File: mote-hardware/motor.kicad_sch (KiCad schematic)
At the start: 1 part, among them U3 TB6612FNG

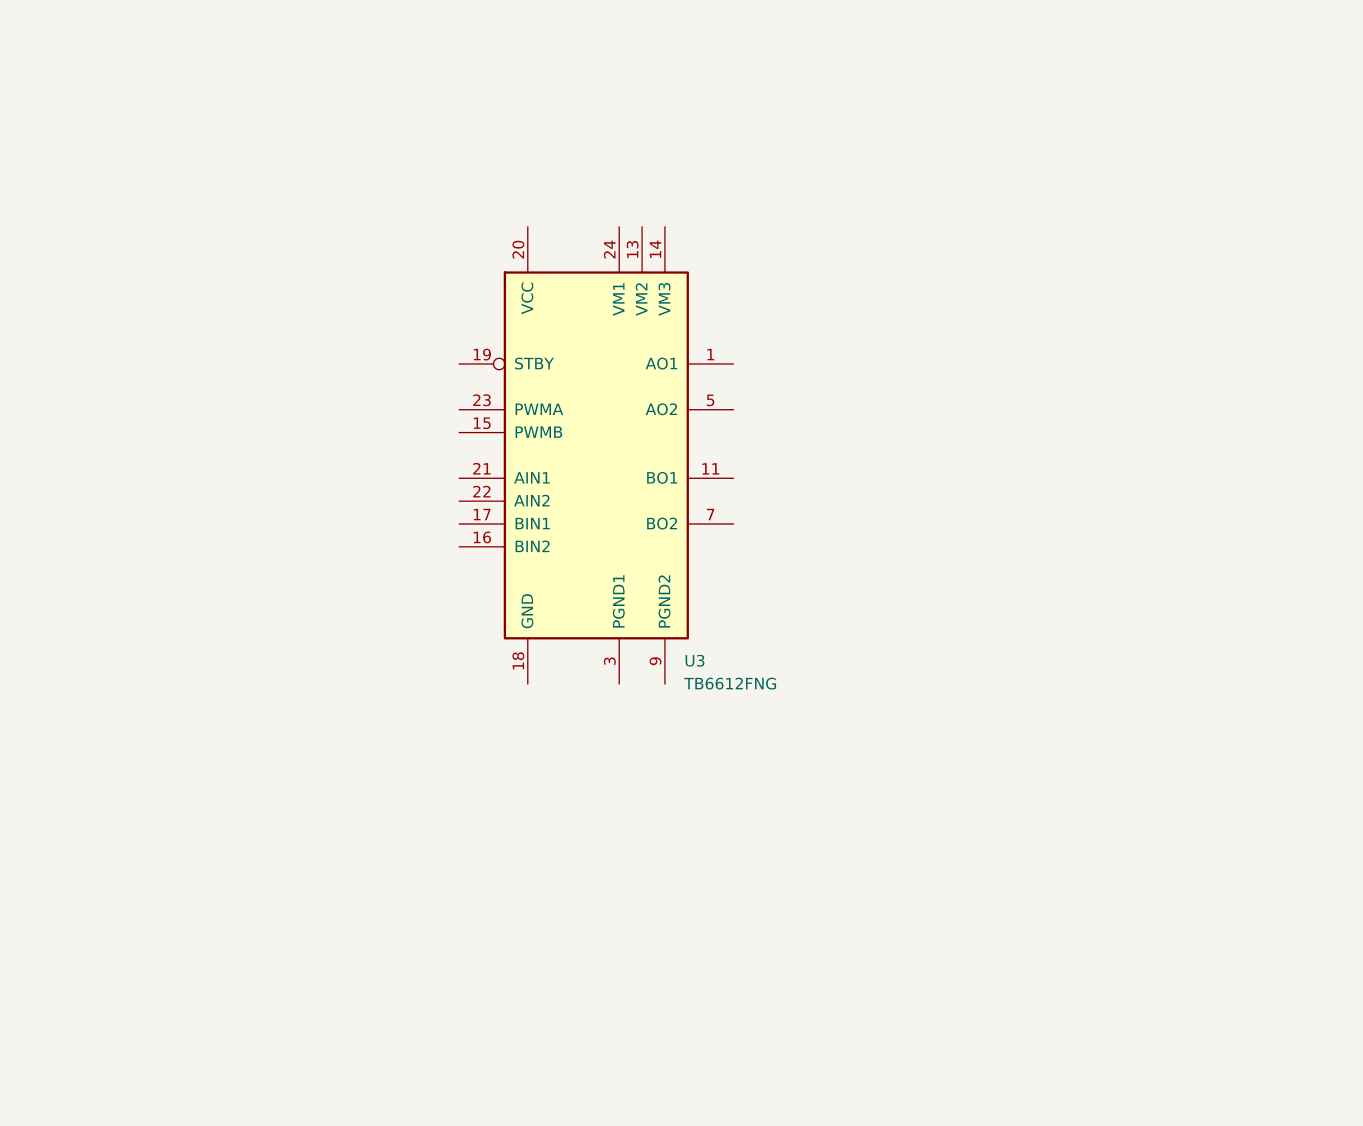
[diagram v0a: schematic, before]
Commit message: Implement motor, power, imu, status LED schematics
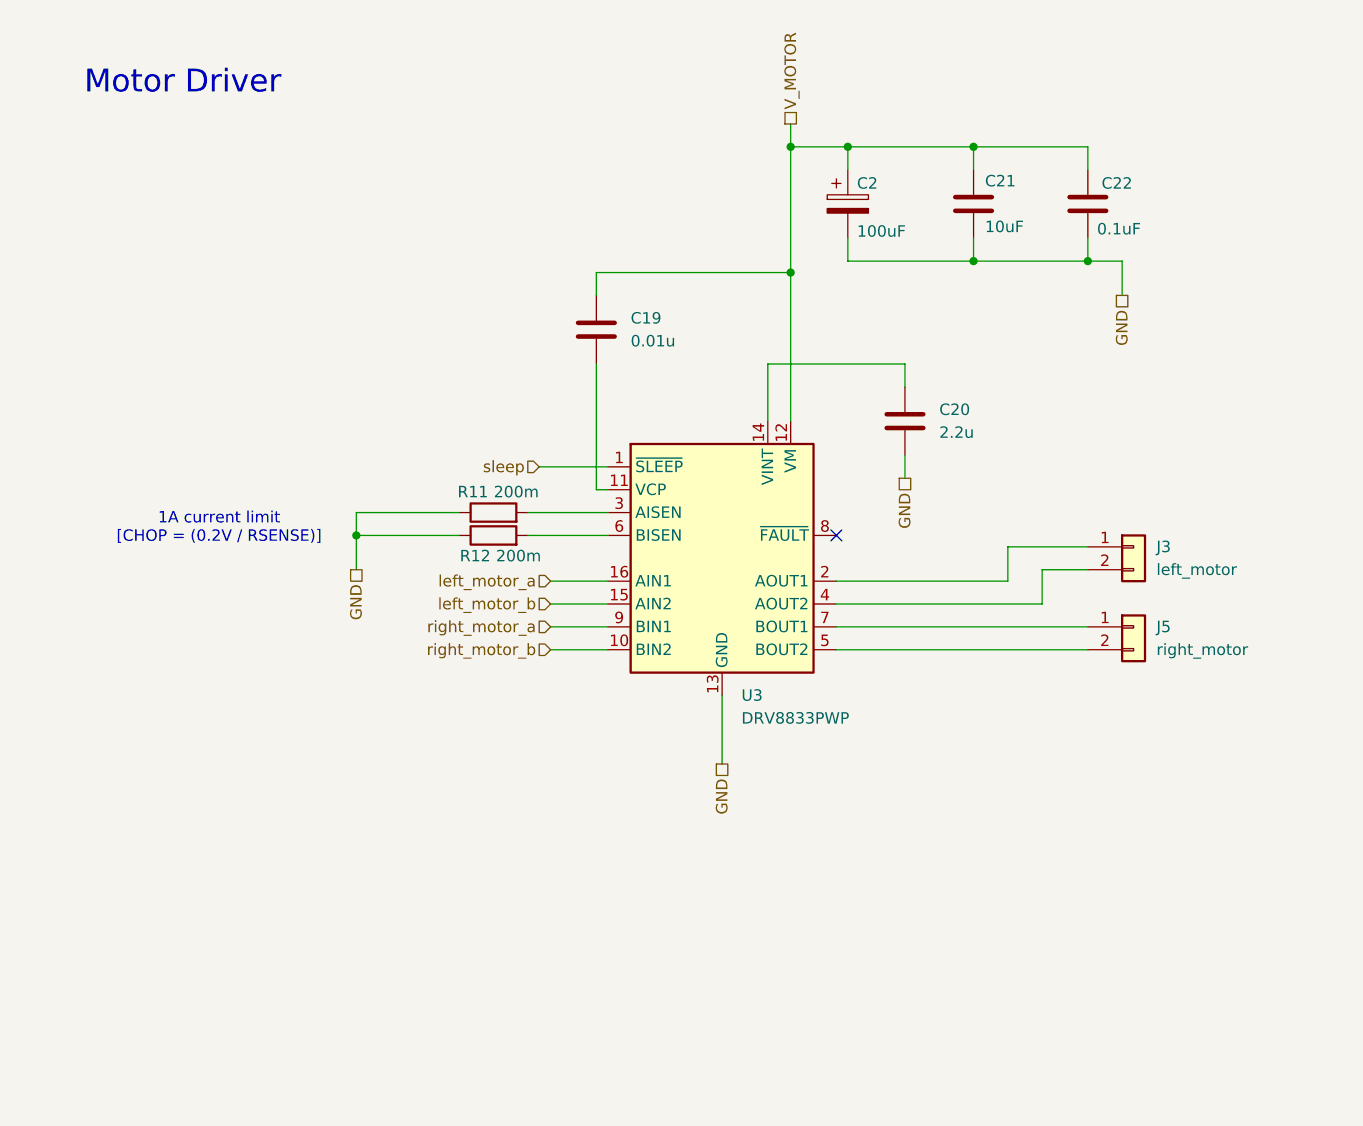
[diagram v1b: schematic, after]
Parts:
- removed U3: TB6612FNG, Package_SO:SSOP-24_5.3x8.2mm_P0.65mm, symbol Driver_Motor:TB6612FNG
- added C19: 0.01u, symbol Device:C
- added C2: 100uF, symbol Device:C_Polarized
- added C20: 2.2u, symbol Device:C
- added C21: 10uF, symbol Device:C
- added C22: 0.1uF, symbol Device:C
- added J3: left_motor, symbol Connector_Generic:Conn_01x02
- added J5: right_motor, symbol Connector_Generic:Conn_01x02
- added R11, R12: 200m, symbol Device:R
- added U3: DRV8833PWP, Package_SO:HTSSOP-16-1EP_4.4x5mm_P0.65mm_EP3.4x5mm_Mask2.46x2.31mm_ThermalVias, symbol Driver_Motor:DRV8833PWP
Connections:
- new net: J3.1 (Pin_1), U3.2 (AOUT1)
- new net: J3.2 (Pin_2), U3.4 (AOUT2)
- new net: R12.2, U3.6 (BISEN)
- new net: J5.1 (Pin_1), U3.7 (BOUT1)
- new net: J5.2 (Pin_2), U3.5 (BOUT2)
- new net: C19.1, U3.11 (VCP)
- new net: C20.2, U3.14 (VINT)
- new net: R11.2, U3.3 (AISEN)
- new net GND: C2.2, C20.1, C21.1, C22.1, R11.1, R12.1, U3.13 (GND), U3.17 (GND)
- new net V_MOTOR: C19.2, C2.1, C21.2, C22.2, U3.12 (VM)
- new net left_motor_a: U3.16 (AIN1)
- new net left_motor_b: U3.15 (AIN2)
- new net right_motor_a: U3.9 (BIN1)
- new net right_motor_b: U3.10 (BIN2)
- new net sleep: U3.1 (~{SLEEP})
- no-connect marks 0 -> 1
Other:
- note added: "1A current limit [CHOP = (0.2V / RSENSE)]"
- note added: "Motor Driver"

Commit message: First draft schematic complete
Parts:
- removed J3: left_motor, symbol Connector_Generic:Conn_01x02
- removed J5: right_motor, symbol Connector_Generic:Conn_01x02
- added J7: left_motor, symbol Connector_Generic:Conn_01x06
- added J8: right_motor, symbol Connector_Generic:Conn_01x06
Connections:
- net GND: now also J7.1 (Pin_1), J8.1 (Pin_1)
- net at U3.2 (AOUT1): now also J7.5 (Pin_5)
- net at U3.4 (AOUT2): now also J7.6 (Pin_6)
- net at U3.7 (BOUT1): now also J8.5 (Pin_5)
- net at U3.5 (BOUT2): now also J8.6 (Pin_6)
- new net +3v3: J7.4 (Pin_4), J8.4 (Pin_4)
- new net left_encoder_a: J7.2 (Pin_2)
- new net left_encoder_b: J7.3 (Pin_3)
- new net right_encoder_a: J8.2 (Pin_2)
- new net right_encoder_b: J8.3 (Pin_3)
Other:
- note added: "Need mounting connectors for motors"
- company: (none) -> github.com/usedhondacivic/mote
- title: (none) -> Mote
- moved on the sheet: C20

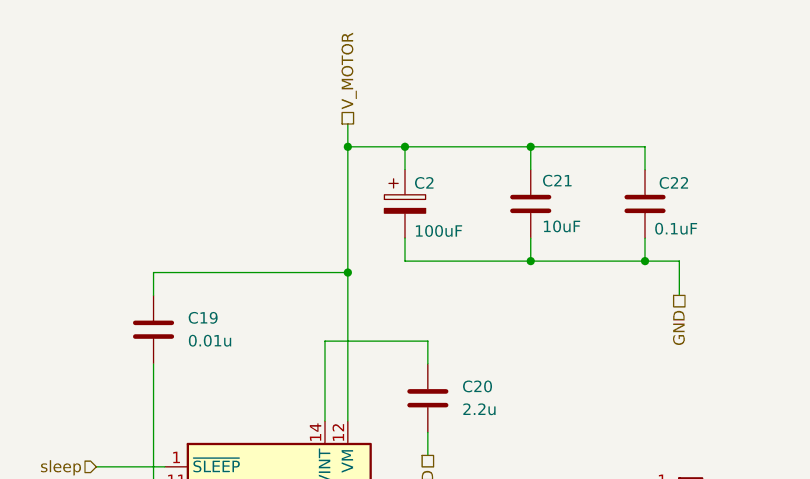
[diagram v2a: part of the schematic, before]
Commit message: Footprint assignments
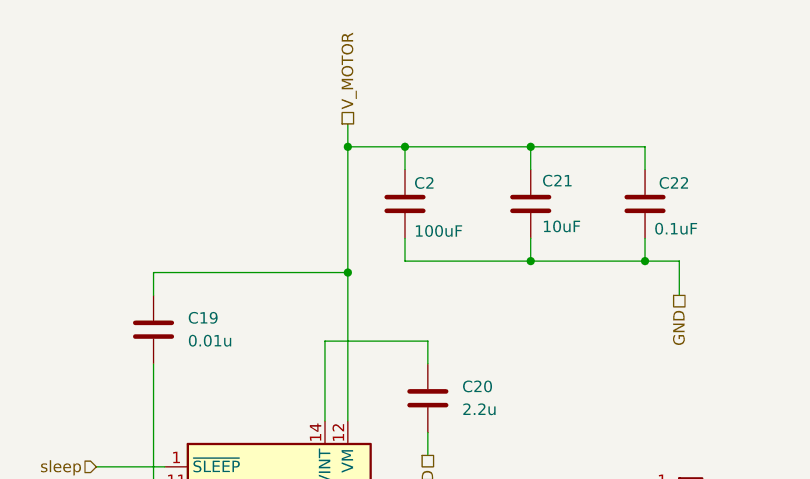
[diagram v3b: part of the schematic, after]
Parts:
- C19, C20, C22: footprint (none) -> Capacitor_SMD:C_0402_1005Metric
- C2: footprint (none) -> Capacitor_SMD:C_1206_3216Metric; symbol Device:C_Polarized -> Device:C
- C21: footprint (none) -> Capacitor_SMD:C_0805_2012Metric
- J7, J8: footprint (none) -> Connector_JST:JST_PH_B6B-PH-K_1x06_P2.00mm_Vertical
- R11, R12: footprint (none) -> Resistor_SMD:R_0402_1005Metric
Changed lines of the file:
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@@
 	)
 	(symbol
-		(lib_id "Device:C_Polarized")
+		(lib_id "Device:C")
 		(at 166.37 67.31 0)
 		(unit 1)
@@
 			)
 		)
-		(property "Footprint" ""
+		(property "Footprint" "Capacitor_SMD:C_1206_3216Metric"
 			(at 167.3352 71.12 0)
 			(effects
@@
 			)
 		)
-		(property "Description" "Polarized capacitor"
+		(property "Description" "Unpolarized capacitor"
 			(at 166.37 67.31 0)
 			(effects
@@
 			)
 		)
-		(property "Footprint" ""
+		(property "Footprint" "Capacitor_SMD:C_0805_2012Metric"
 			(at 179.3748 63.5 0)
 			(effects
@@
 			)
 		)
-		(property "Footprint" ""
+		(property "Footprint" "Capacitor_SMD:C_0402_1005Metric"
 			(at 192.0748 63.5 0)
 			(effects
@@
 			)
 		)
-		(property "Footprint" ""
+		(property "Footprint" "Connector_JST:JST_PH_B6B-PH-K_1x06_P2.00mm_Vertical"
 			(at 198.12 125.73 0)
 			(effects
@@
 			)
 		)
-		(property "Footprint" ""
+		(property "Footprint" "Connector_JST:JST_PH_B6B-PH-K_1x06_P2.00mm_Vertical"
 			(at 198.12 104.14 0)
 			(effects
@@
 			)
 		)
-		(property "Footprint" ""
+		(property "Footprint" "Resistor_SMD:R_0402_1005Metric"
 			(at 127 105.918 90)
 			(effects
@@
 			)
 		)
-		(property "Footprint" ""
+		(property "Footprint" "Capacitor_SMD:C_0402_1005Metric"
 			(at 137.4648 77.47 0)
 			(effects
@@
 			)
 		)
-		(property "Footprint" ""
+		(property "Footprint" "Resistor_SMD:R_0402_1005Metric"
 			(at 127 103.378 90)
 			(effects
@@
 			)
 		)
-		(property "Footprint" ""
+		(property "Footprint" "Capacitor_SMD:C_0402_1005Metric"
 			(at 167.9448 85.09 0)
 			(effects

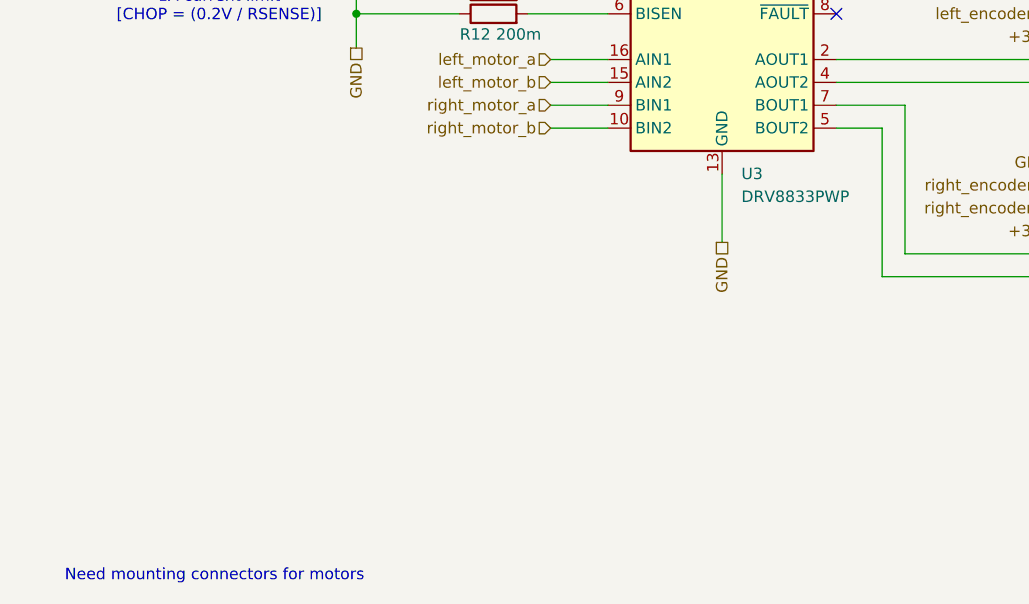
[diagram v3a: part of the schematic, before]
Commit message: Get pcb ready for first prototype order (#31)
Co-authored-by: Kyle Mui <44453997+KyleMui@users.noreply.github.com>
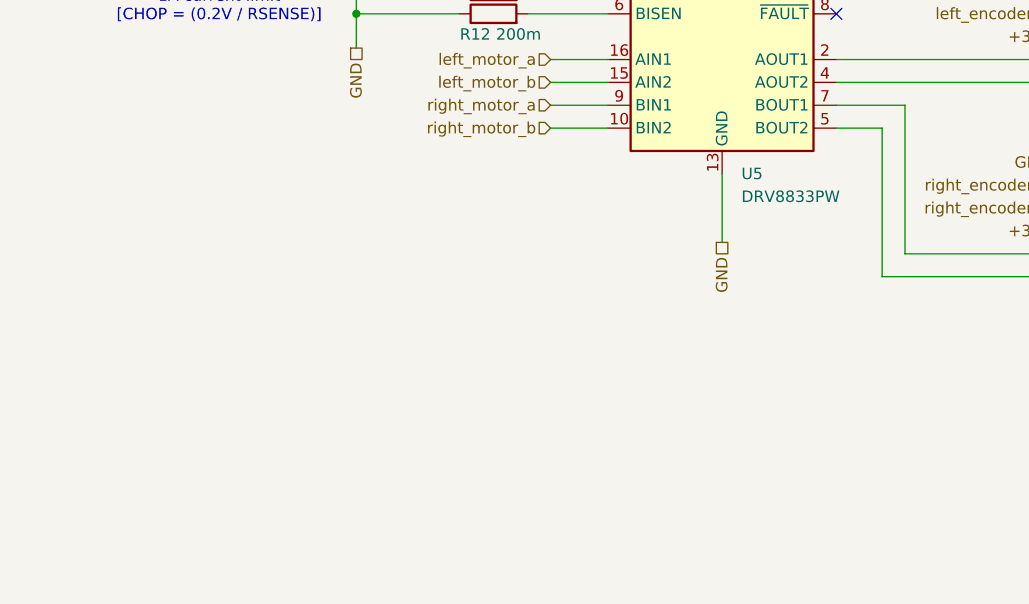
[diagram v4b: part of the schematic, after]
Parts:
- removed U3: DRV8833PWP, Package_SO:HTSSOP-16-1EP_4.4x5mm_P0.65mm_EP3.4x5mm_Mask2.46x2.31mm_ThermalVias, symbol Driver_Motor:DRV8833PWP
- added U5: DRV8833PW, Package_SO:TSSOP-16-1EP_4.4x5mm_P0.65mm, symbol Driver_Motor:DRV8833PW
- C19, C20, C22: footprint Capacitor_SMD:C_0402_1005Metric -> PCM_JLCPCB:C_0402
- C2: footprint Capacitor_SMD:C_1206_3216Metric -> PCM_JLCPCB:C_1206
- C21: footprint Capacitor_SMD:C_0805_2012Metric -> PCM_JLCPCB:C_0805
- R11, R12: footprint Resistor_SMD:R_0402_1005Metric -> PCM_JLCPCB:R_0402
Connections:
- net GND: now also U5.13 (GND)
- net V_MOTOR: now also U5.12 (VM)
- net left_motor_a: now also U5.16 (AIN1)
- net left_motor_b: now also U5.15 (AIN2)
- net right_motor_a: now also U5.9 (BIN1)
- net right_motor_b: now also U5.10 (BIN2)
- net sleep: now also U5.1 (~{SLEEP})
- net at J8.5 (Pin_5): now also U5.7 (BOUT1)
- net at J8.6 (Pin_6): now also U5.5 (BOUT2)
- net at J7.5 (Pin_5): now also U5.2 (AOUT1)
- net at J7.6 (Pin_6): now also U5.4 (AOUT2)
- net at R12.2: now also U5.6 (BISEN)
- net at C19.1: now also U5.11 (VCP)
- net at C20.2: now also U5.14 (VINT)
- net at R11.2: now also U5.3 (AISEN)
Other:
- note removed: "Need mounting connectors for motors"
- company: github.com/usedhondacivic/mote -> github.com/empriselab/mote-core
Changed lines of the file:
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@@
 	(title_block
 		(title "Mote")
-		(date "2025-12-30")
+		(date "2026-03-31")
 		(rev "V0.0.0")
-		(company "github.com/usedhondacivic/mote")
-	)
-	(text "Need mounting connectors for motors"
-		(exclude_from_sim no)
-		(at 96.012 166.624 0)
-		(effects
-			(font
-				(size 1.27 1.27)
-			)
-		)
+		(company "github.com/empriselab/mote-core")
 	)
 	(text "1A current limit\n[CHOP = (0.2V / RSENSE)]"
@@
 			)
 		)
-		(property "Footprint" "Capacitor_SMD:C_1206_3216Metric"
+		(property "Footprint" "PCM_JLCPCB:C_1206"
 			(at 167.3352 71.12 0)
 			(effects
@@
 		)
 		(instances
-			(project ""
+			(project "mote-hardware"
 				(path "/94683f5c-9cd9-448e-be96-9792537b5cb8/332292ea-bd81-44ca-9f8d-1cb79fb18ef4"
 					(reference "C2")
@@
 			)
 		)
-		(property "Footprint" "Capacitor_SMD:C_0805_2012Metric"
+		(property "Footprint" "PCM_JLCPCB:C_0805"
 			(at 179.3748 63.5 0)
 			(effects
@@
 			)
 		)
-		(property "Footprint" "Capacitor_SMD:C_0402_1005Metric"
+		(property "Footprint" "PCM_JLCPCB:C_0402"
 			(at 192.0748 63.5 0)
 			(effects
@@
 		)
 		(instances
-			(project ""
+			(project "mote-hardware"
 				(path "/94683f5c-9cd9-448e-be96-9792537b5cb8/332292ea-bd81-44ca-9f8d-1cb79fb18ef4"
 					(reference "J7")
@@
 			)
 		)
-		(property "Footprint" "Resistor_SMD:R_0402_1005Metric"
+		(property "Footprint" "PCM_JLCPCB:R_0402"
 			(at 127 105.918 90)
 			(effects
@@
 	)
 	(symbol
-		(lib_id "Driver_Motor:DRV8833PWP")
+		(lib_id "Driver_Motor:DRV8833PW")
 		(at 152.4 106.68 0)
 		(unit 1)
@@
 		(dnp no)
 		(fields_autoplaced yes)
-		(property "Reference" "U3"
+		(property "Reference" "U5"
 			(at 154.5433 121.92 0)
 			(effects
@@
 			)
 		)
-		(property "Value" "DRV8833PWP"
+		(property "Value" "DRV8833PW"
 			(at 154.5433 124.46 0)
 			(effects
@@
 			)
 		)
-		(property "Footprint" "Package_SO:HTSSOP-16-1EP_4.4x5mm_P0.65mm_EP3.4x5mm_Mask2.46x2.31mm_ThermalVias"
-			(at 157.48 121.92 0)
+		(property "Footprint" "Package_SO:TSSOP-16-1EP_4.4x5mm_P0.65mm"
+			(at 157.48 124.46 0)
 			(effects
 				(font
@@
 		)
 		(property "Datasheet" "http://www.ti.com/lit/ds/symlink/drv8833.pdf"
-			(at 157.48 124.46 0)
+			(at 157.48 127 0)
 			(effects
 				(font
@@
 			)
 		)
-		(property "Description" "Dual H-Bridge Motor Driver, HTSSOP-16"
+		(property "Description" "Dual H-Bridge Motor Driver, TSSOP-16"
 			(at 152.4 106.68 0)
 			(effects
@@
 			)
 		)
+		(pin "10"
+		)
 		(pin "13"
 		)
+		(pin "12"
+		)
+		(pin "8"
+		)
+		(pin "4"
+		)
+		(pin "2"
+		)
+		(pin "14"
+		)
+		(pin "7"
+		)
+		(pin "6"
+		)
+		(pin "5"
+		)
 		(pin "11"
 		)
 		(pin "1"
 		)
+		(pin "15"
+		)
+		(pin "9"
+		)
+		(pin "16"
+		)
 		(pin "3"
 		)
-		(pin "14"
-		)
-		(pin "9"
-		)
-		(pin "2"
-		)
-		(pin "17"
-		)
-		(pin "10"
-		)
-		(pin "15"
-		)
-		(pin "7"
-		)
-		(pin "8"
-		)
-		(pin "12"
-		)
-		(pin "5"
-		)
-		(pin "4"
-		)
-		(pin "6"
-		)
-		(pin "16"
-		)
 		(instances
-			(project ""
+			(project "mote-hardware"
 				(path "/94683f5c-9cd9-448e-be96-9792537b5cb8/332292ea-bd81-44ca-9f8d-1cb79fb18ef4"
-					(reference "U3")
+					(reference "U5")
 					(unit 1)
 				)
@@
 			)
 		)
-		(property "Footprint" "Capacitor_SMD:C_0402_1005Metric"
+		(property "Footprint" "PCM_JLCPCB:C_0402"
 			(at 137.4648 77.47 0)
 			(effects
@@
 			)
 		)
-		(property "Footprint" "Resistor_SMD:R_0402_1005Metric"
+		(property "Footprint" "PCM_JLCPCB:R_0402"
 			(at 127 103.378 90)
 			(effects
@@
 		)
 		(instances
-			(project ""
+			(project "mote-hardware"
 				(path "/94683f5c-9cd9-448e-be96-9792537b5cb8/332292ea-bd81-44ca-9f8d-1cb79fb18ef4"
 					(reference "R11")
@@
 			)
 		)
-		(property "Footprint" "Capacitor_SMD:C_0402_1005Metric"
+		(property "Footprint" "PCM_JLCPCB:C_0402"
 			(at 167.9448 85.09 0)
 			(effects

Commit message: Fix DRC warnings
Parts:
- J7: value left_motor -> JST_PH_B6B
- J8: value right_motor -> JST_PH_B6B
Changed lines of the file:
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@@
 			)
 		)
-		(property "Value" "right_motor"
+		(property "Value" "JST_PH_B6B"
 			(at 200.66 128.2699 0)
 			(effects
@@
 			)
 		)
-		(property "Value" "left_motor"
+		(property "Value" "JST_PH_B6B"
 			(at 200.66 106.6799 0)
 			(effects
